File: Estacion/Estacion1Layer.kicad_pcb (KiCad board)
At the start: 2 copper layers, 120 x 62.2 mm, 12 parts, among them SW1 SW_Push, U4 WeMos_S2_mini, U5 DHT22, U6 FN-M16P

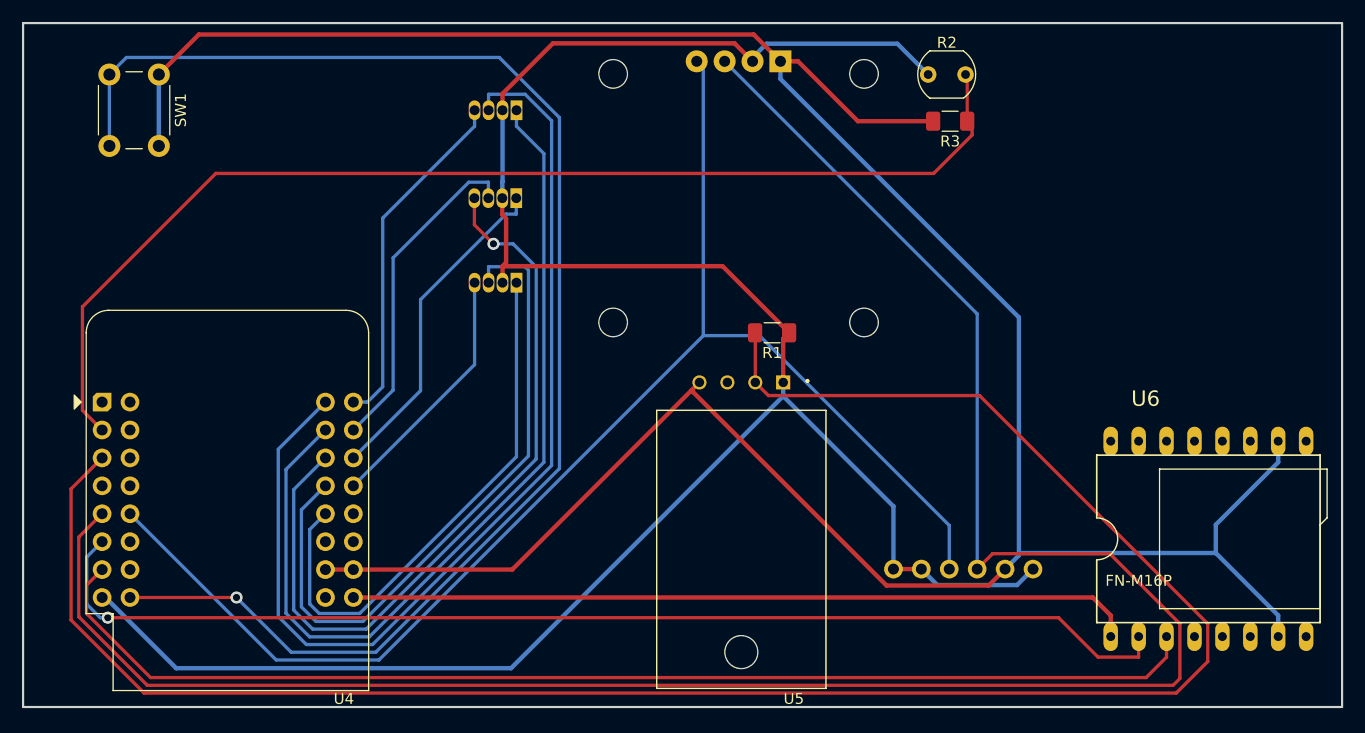
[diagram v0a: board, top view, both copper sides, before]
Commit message: Añadir versiones de pcb para dos capas y una capa
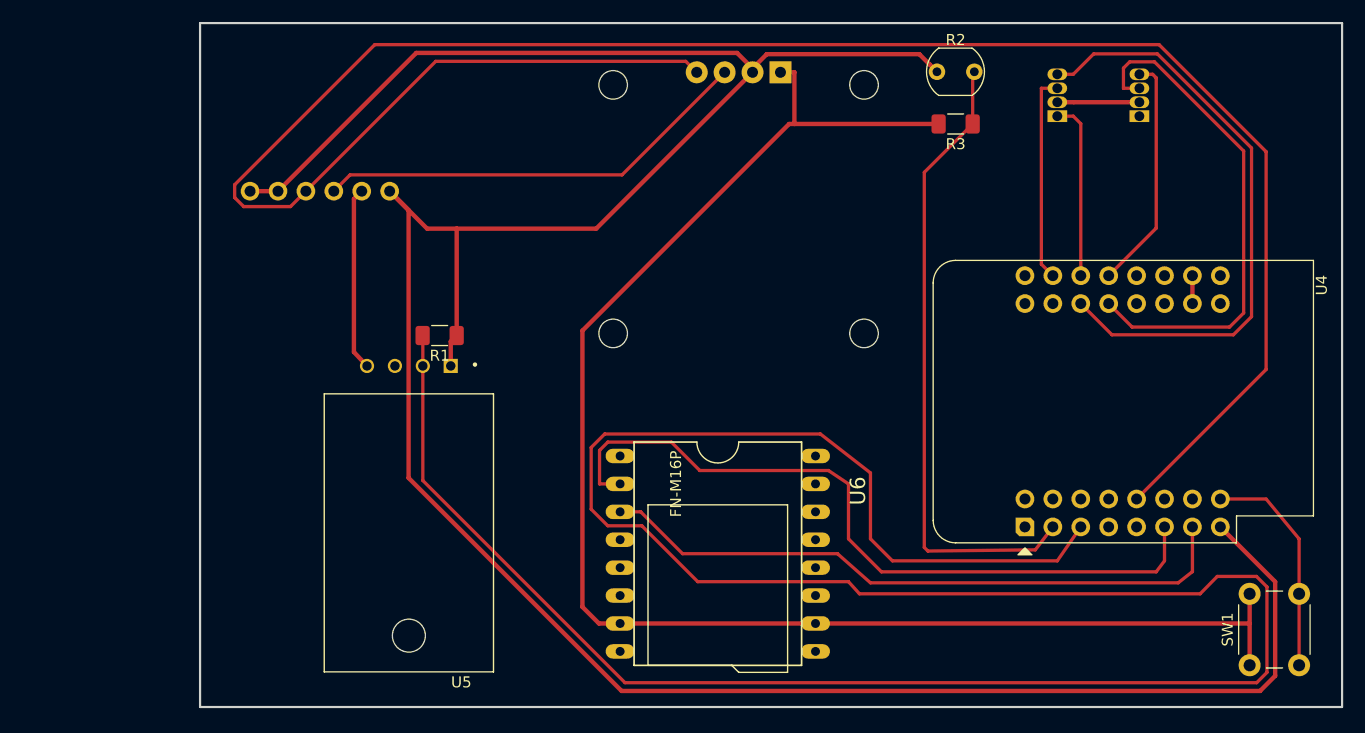
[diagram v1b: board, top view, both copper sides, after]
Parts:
- removed D5: LED_RABG, LED_THT:LED_D5.0mm-4_RGB
- BMP280: moved to B.Cu
- moved SW1 112.9 mm to (176.5, 110.5), turned to 90 degrees
- moved U4 84.7 mm to (156.1, 97.9), turned to 90 degrees
- moved BMP280 67.9 mm to (98.2, 67.4), turned to 90 degrees
- moved D3 58.7 mm to (166.5, 60.5), turned to 90 degrees
- moved D4 49.8 mm to (159.0, 60.5), turned to 90 degrees
- moved U6 44.7 mm to (128.1, 100.3), turned to -90 degrees
- moved U5 30.3 mm to (100.0, 98.5)
- moved R1 30.3 mm to (102.8, 80.5)
- moved D1 1.00 mm to (130.0, 69.2)
- moved R2 0.84 mm to (148.1, 56.5)
- moved R3 0.56 mm to (149.8, 61.2)
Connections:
- U4 pad 16: Net-(D5-GK) -> unconnected-(U4-GPIO39-Pad16)
- U4 pad 31: Net-(D5-RK) -> unconnected-(U4-GPIO38-Pad31)
- U4 pad 32: Net-(D5-BK) -> unconnected-(U4-GPIO40-Pad32)
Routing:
- net /SCL: track 195.6 -> 40.0 mm
- net Net-(U4-GPIO14): track 130.4 -> 20.4 mm, vias 1 -> 0
- net GND: track 255.4 -> 158.3 mm
- net Net-(D5-BK): track 93.5 -> 0.00 mm
- net Net-(D5-RK): track 82.2 -> 0.00 mm
- net +5V: track 71.5 -> 0.00 mm
- net /SDA: track 128.6 -> 189.1 mm
- net +3V3: track 204.1 -> 260.2 mm
- net Net-(U4-GPIO5): track 181.5 -> 231.9 mm
- net Net-(D3-RK): track 49.7 -> 0.00 mm
- net Net-(U4-GPIO12): track 107.9 -> 59.1 mm
- net Net-(U4-GPIO3): track 105.1 -> 58.0 mm
- net Net-(U4-GPIO11): track 105.8 -> 67.9 mm, vias 1 -> 0
- net Net-(D5-GK): track 31.9 -> 0.00 mm
- net Net-(D4-GK): track 71.3 -> 54.7 mm, vias 1 -> 0
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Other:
- board size 120 x 62.2 mm -> 103.9 x 62.2 mm
